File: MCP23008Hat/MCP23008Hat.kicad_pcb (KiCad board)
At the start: 2 copper layers, 65 x 56 mm, 11 parts, among them J0 RPi_GPIO, J1 Address, T1 GPIO, U1 MCP23008

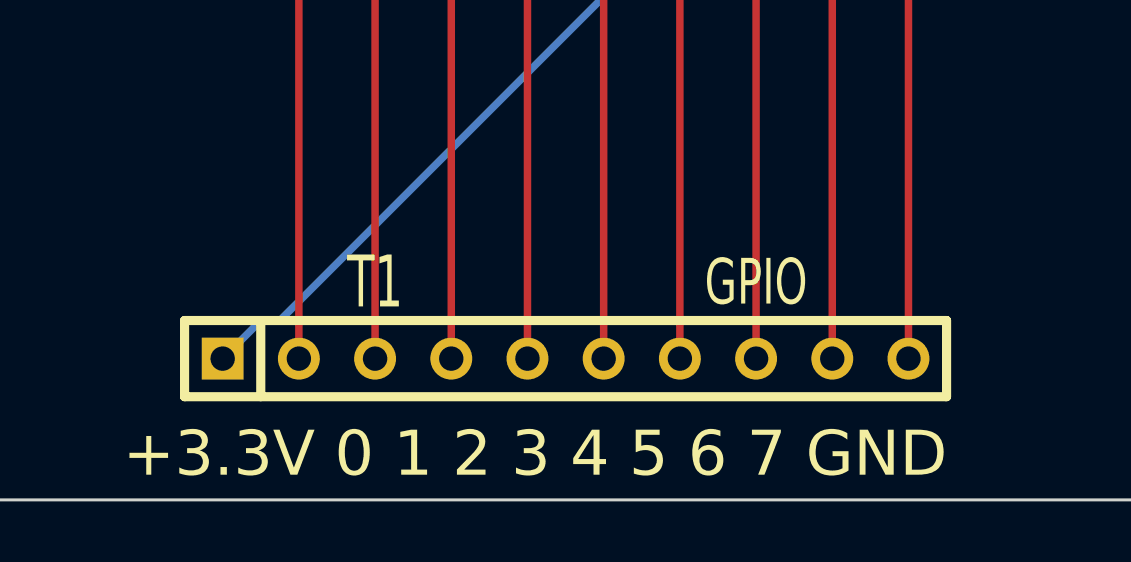
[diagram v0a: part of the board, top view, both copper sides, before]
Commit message: Update screw terminals on all HATs.
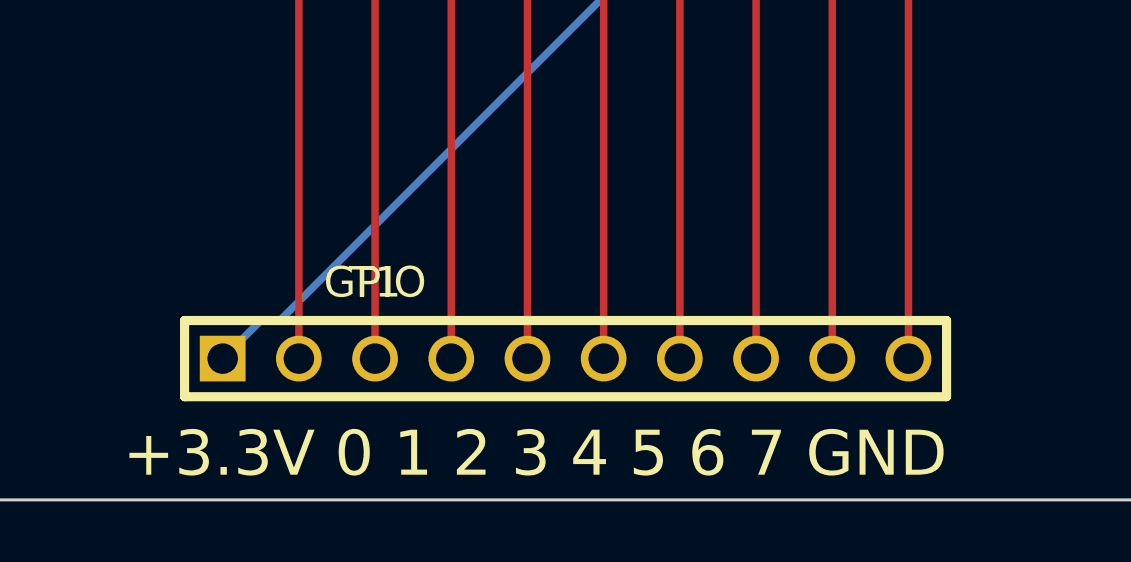
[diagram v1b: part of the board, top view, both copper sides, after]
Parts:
- T1: footprint SIL-10 -> PIN_ARRAY_5x1
- moved T1 6.35 mm to (67.3, 83.2)
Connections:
- T1 pad 10: GND -> (no net)
- T1 pad 6: N-0000014 -> (no net)
- T1 pad 7: N-0000015 -> (no net)
- T1 pad 8: N-0000016 -> (no net)
- T1 pad 9: N-0000017 -> (no net)
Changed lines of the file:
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@@
 (kicad_pcb (version 3) (host pcbnew "(2013-june-11)-stable")
   (general
-    (links 35)
-    (no_connects 0)
+    (links 30)
+    (no_connects 5)
     (area 28.812572 20.694 130.847429 101.769)
     (thickness 1.6)
@@
     (mod_text_size 1 1)
     (mod_text_width 0.15)
-    (pad_size 2.75 2.75)
-    (pad_drill 2.75)
+    (pad_size 1.524 1.524)
+    (pad_drill 1.016)
     (pad_to_mask_clearance 0)
     (aux_axis_origin 0 0)
@@
     (add_net N-000006)
   )
-  (module SIL-10   placed (layer F.Cu)
-    (at 73.66 83.185)
-    (descr "Connecteur 10 pins")
-    (tags "CONN DEV")
-    (fp_text reference T1 (at -6.35 -2.54) (layer F.SilkS)
-      (effects (font (size 1.72974 1.08712) (thickness 0.3048)))
+  (module PIN_ARRAY_5x1 (layer F.Cu)
+    (at 67.31 83.185)
+    (descr "Double rangee de contacts 2 x 5 pins")
+    (tags CONN)
+    (fp_text reference T1 (at 0 -2.54) (layer F.SilkS)
+      (effects (font (size 1.016 1.016) (thickness 0.2032)))
     )
-    (fp_text value GPIO (at 6.35 -2.54) (layer F.SilkS)
-      (effects (font (size 1.524 1.016) (thickness 0.254)))
+    (fp_text value GPIO (at 0 -2.54) (layer F.SilkS)
+      (effects (font (size 1.016 1.016) (thickness 0.2032)))
     )
-    (fp_line (start -12.7 1.27) (end -12.7 -1.27) (layer F.SilkS) (width 0.3048))
-    (fp_line (start -12.7 -1.27) (end 12.7 -1.27) (layer F.SilkS) (width 0.3048))
-    (fp_line (start 12.7 -1.27) (end 12.7 1.27) (layer F.SilkS) (width 0.3048))
-    (fp_line (start 12.7 1.27) (end -12.7 1.27) (layer F.SilkS) (width 0.3048))
-    (fp_line (start -10.16 1.27) (end -10.16 -1.27) (layer F.SilkS) (width 0.3048))
-    (pad 1 thru_hole rect (at -11.43 0) (size 1.397 1.397) (drill 0.8128)
+    (fp_line (start -6.35 -1.27) (end -6.35 1.27) (layer F.SilkS) (width 0.3048))
+    (fp_line (start 19.05 1.27) (end 19.05 -1.27) (layer F.SilkS) (width 0.3048))
+    (fp_line (start -6.35 -1.27) (end 19.05 -1.27) (layer F.SilkS) (width 0.3048))
+    (fp_line (start 19.05 1.27) (end -6.35 1.27) (layer F.SilkS) (width 0.3048))
+    (pad 1 thru_hole rect (at -5.08 0) (size 1.524 1.524) (drill 1.016)
       (layers *.Cu *.Mask F.SilkS)
       (net 1 +3.3V)
     )
-    (pad 2 thru_hole circle (at -8.89 0) (size 1.397 1.397) (drill 0.8128)
+    (pad 2 thru_hole circle (at -2.54 0) (size 1.524 1.524) (drill 1.016)
       (layers *.Cu *.Mask F.SilkS)
       (net 6 N-0000010)
     )
-    (pad 3 thru_hole circle (at -6.35 0) (size 1.397 1.397) (drill 0.8128)
+    (pad 3 thru_hole circle (at 0 0) (size 1.524 1.524) (drill 1.016)
       (layers *.Cu *.Mask F.SilkS)
       (net 7 N-0000011)
     )
-    (pad 4 thru_hole circle (at -3.81 0) (size 1.397 1.397) (drill 0.8128)
+    (pad 4 thru_hole circle (at 2.54 0) (size 1.524 1.524) (drill 1.016)
       (layers *.Cu *.Mask F.SilkS)
       (net 8 N-0000012)
     )
-    (pad 5 thru_hole circle (at -1.27 0) (size 1.397 1.397) (drill 0.8128)
+    (pad 5 thru_hole circle (at 5.08 0) (size 1.524 1.524) (drill 1.016)
       (layers *.Cu *.Mask F.SilkS)
       (net 9 N-0000013)
     )
-    (pad 6 thru_hole circle (at 1.27 0) (size 1.397 1.397) (drill 0.8128)
+    (pad 6 thru_hole circle (at 7.62 0) (size 1.524 1.524) (drill 1.016)
       (layers *.Cu *.Mask F.SilkS)
-      (net 10 N-0000014)
     )
-    (pad 7 thru_hole circle (at 3.81 0) (size 1.397 1.397) (drill 0.8128)
+    (pad 7 thru_hole circle (at 10.16 0) (size 1.524 1.524) (drill 1.016)
       (layers *.Cu *.Mask F.SilkS)
-      (net 11 N-0000015)
     )
-    (pad 8 thru_hole circle (at 6.35 0) (size 1.397 1.397) (drill 0.8128)
+    (pad 8 thru_hole circle (at 12.7 0) (size 1.524 1.524) (drill 1.016)
       (layers *.Cu *.Mask F.SilkS)
-      (net 12 N-0000016)
     )
-    (pad 9 thru_hole circle (at 8.89 0) (size 1.397 1.397) (drill 0.8128)
+    (pad 9 thru_hole circle (at 15.24 0) (size 1.524 1.524) (drill 1.016)
       (layers *.Cu *.Mask F.SilkS)
-      (net 13 N-0000017)
     )
-    (pad 10 thru_hole circle (at 11.43 0) (size 1.397 1.397) (drill 0.8128)
+    (pad 10 thru_hole circle (at 17.78 0) (size 1.524 1.524) (drill 1.016)
       (layers *.Cu *.Mask F.SilkS)
-      (net 4 GND)
     )
-    (model device/bornier_5.wrl
+    (model walter/conn_screw/mors_10p.wrl
       (at (xyz 0.25 0 0))
       (scale (xyz 0.5 0.5 0.5))
-      (rotate (xyz 0 0 0))
-    )
-    (model device/bornier_5.wrl
-      (at (xyz -0.25 0 0))
-      (scale (xyz 0.5 0.5 0.5))
-      (rotate (xyz 0 0 0))
+      (rotate (xyz 0 0 180))
     )
   )
